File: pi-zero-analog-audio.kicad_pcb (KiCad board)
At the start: 2 copper layers, 65 x 30 mm, 29 parts, among them J1 GPIO, J2 SJ1-3555NG-BE, J3 Screw_Terminal_01x04, U1 LP5907MFX-3.3, U2 74LVC2G34, U3 PAM8403D

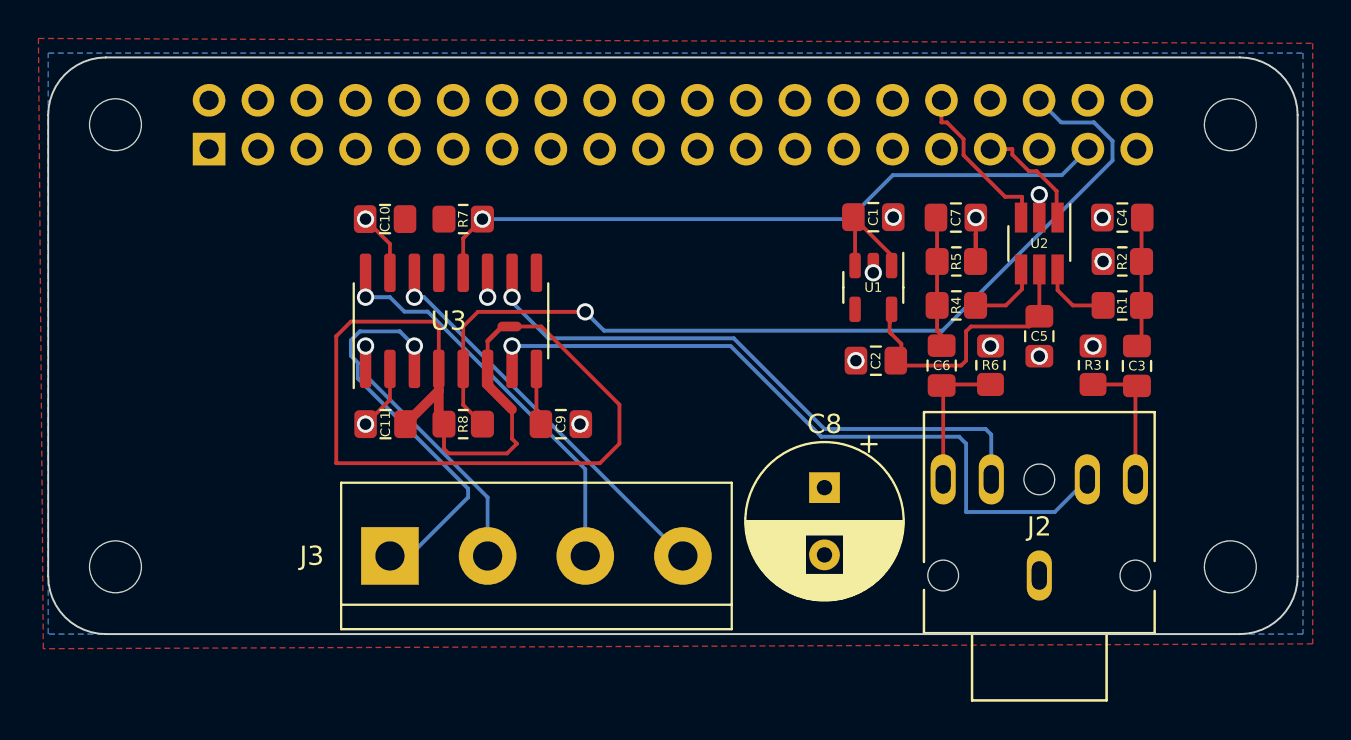
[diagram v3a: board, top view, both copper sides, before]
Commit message: Clearing the mounting holes to avoid accidental short
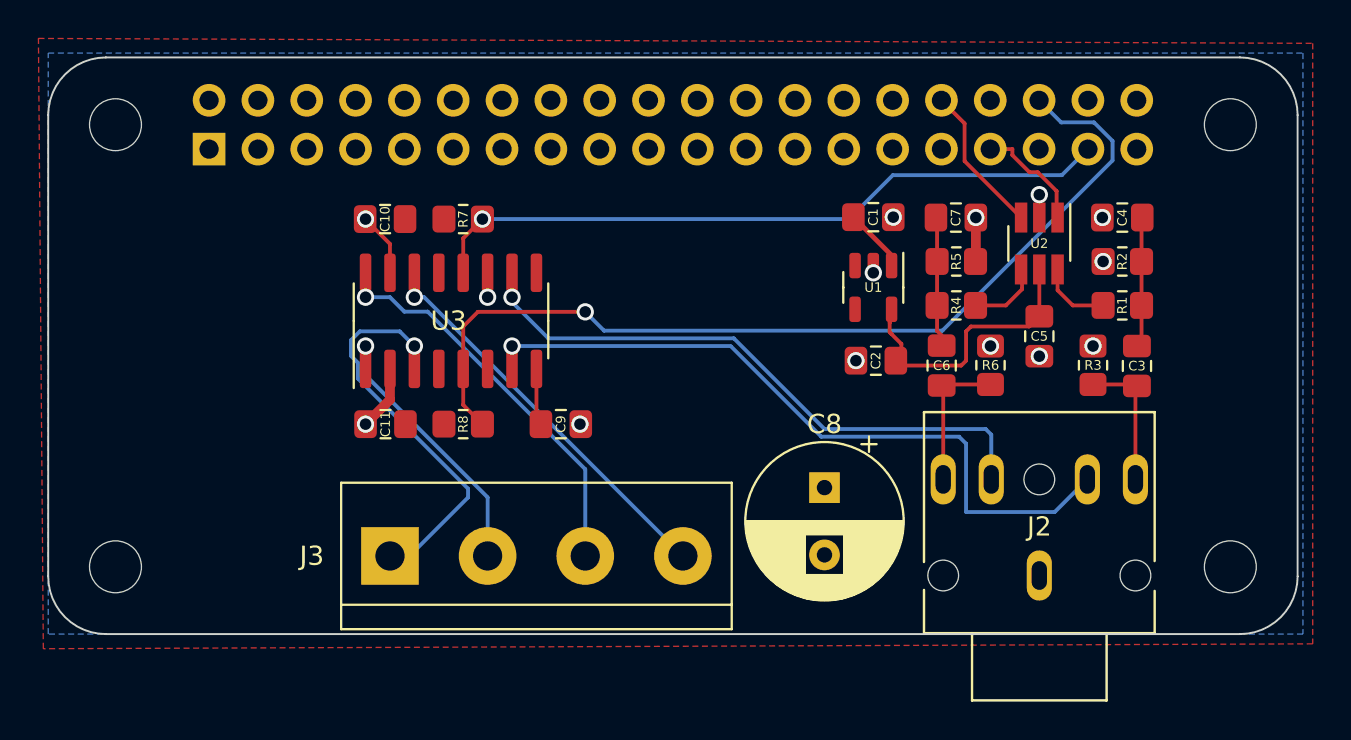
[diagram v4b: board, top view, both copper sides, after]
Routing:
- net +5V: track 62.6 -> 2.81 mm
- net GND: track 9.85 -> 8.98 mm
- net /PWM0: track 8.52 -> 7.82 mm
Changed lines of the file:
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@@
     (fp_circle (center 0 0) (end 2.7 0) (layer "Cmts.User") (width 0.15) (fill none))
     (fp_circle (center 0 0) (end 2.95 0) (layer "F.CrtYd") (width 0.05) (fill none))
-    (pad "" np_thru_hole circle locked (at 0 0) (size 2.7 2.7) (drill 2.7) (layers *.Cu *.Mask))
+    (pad "" np_thru_hole circle locked (at 0 0) (size 2.7 2.7) (drill 2.7) (layers F&B.Cu *.Mask)
+      (clearance 1.625))
   )
   (footprint "Capacitor_SMD:C_0805_2012Metric_Pad1.18x1.45mm_HandSolder" (layer "F.Cu")
@@
     (fp_circle (center 0 0) (end 2.7 0) (layer "Cmts.User") (width 0.15) (fill none))
     (fp_circle (center 0 0) (end 2.95 0) (layer "F.CrtYd") (width 0.05) (fill none))
-    (pad "" np_thru_hole circle locked (at 0 0) (size 2.7 2.7) (drill 2.7) (layers *.Cu *.Mask))
+    (pad "" np_thru_hole circle locked (at 0 0) (size 2.7 2.7) (drill 2.7) (layers F&B.Cu *.Mask)
+      (clearance 1.625))
   )
   (footprint "MountingHole:MountingHole_2.7mm_M2.5" locked (layer "F.Cu")
@@
     (fp_circle (center 0 0) (end 2.7 0) (layer "Cmts.User") (width 0.15) (fill none))
     (fp_circle (center 0 0) (end 2.95 0) (layer "F.CrtYd") (width 0.05) (fill none))
-    (pad "" np_thru_hole circle locked (at 0 0) (size 2.7 2.7) (drill 2.7) (layers *.Cu *.Mask))
+    (pad "" np_thru_hole circle locked (at 0 0) (size 2.7 2.7) (drill 2.7) (layers F&B.Cu *.Mask)
+      (clearance 1.625))
   )
   (footprint "Package_TO_SOT_SMD:SOT-23-5" (layer "F.Cu")
@@
     (fp_circle (center 0 0) (end 2.7 0) (layer "Cmts.User") (width 0.15) (fill none))
     (fp_circle (center 0 0) (end 2.95 0) (layer "F.CrtYd") (width 0.05) (fill none))
-    (pad "" np_thru_hole circle locked (at 0 0) (size 2.7 2.7) (drill 2.7) (layers *.Cu *.Mask))
+    (pad "" np_thru_hole circle locked (at 0 0) (size 2.7 2.7) (drill 2.7) (layers F&B.Cu *.Mask)
+      (clearance 1.625))
   )
   (footprint "Capacitor_SMD:C_0805_2012Metric_Pad1.18x1.45mm_HandSolder" (layer "F.Cu")
@@
   (gr_arc (start 100 73) (mid 100.87868 70.87868) (end 103 70) (layer "Edge.Cuts") (width 0.1))
   (gr_line (start 162 70) (end 103 70) (layer "Edge.Cuts") (width 0.1))
-  (segment (start 148.26 79.1715) (end 148.244 79.1875) (width 0.2) (layer "F.Cu") (net 1))
-  (segment (start 117.78 87.808) (end 116.51 89.078) (width 0.2) (layer "F.Cu") (net 1))
   (segment (start 117.78 79.7015) (end 116.499 78.421) (width 0.2) (layer "F.Cu") (net 1))
-  (segment (start 117.78 86.204) (end 117.78 87.808) (width 0.2) (layer "F.Cu") (net 1))
-  (segment (start 148.244 79.1875) (end 148.244 80.616) (width 0.2) (layer "F.Cu") (net 1))
   (segment (start 117.78 81.204) (end 117.78 79.7015) (width 0.2) (layer "F.Cu") (net 1))
-  (segment (start 148.26 78.33) (end 148.26 79.1715) (width 0.2) (layer "F.Cu") (net 1))
-  (segment (start 148.26 79.1715) (end 148.26 80.013) (width 0.2) (layer "F.Cu") (net 1))
+  (segment (start 148.26 78.33) (end 148.26 80.6) (width 0.508) (layer "F.Cu") (net 1))
+  (segment (start 117.78 86.204) (end 117.78 87.808) (width 0.508) (layer "F.Cu") (net 1))
+  (segment (start 117.78 87.808) (end 116.51 89.078) (width 0.508) (layer "F.Cu") (net 1))
   (via (at 127.6645 89.078) (size 0.9) (drill 0.6) (layers "F.Cu" "B.Cu") (net 1))
   (via (at 154.88 80.616) (size 0.9) (drill 0.6) (layers "F.Cu" "B.Cu") (net 1))
@@
   (segment (start 143.876 84.3961) (end 143.776 84.2961) (width 0.2) (layer "F.Cu") (net 2))
   (segment (start 151.562 83.4685) (end 151.562 81.03) (width 0.2) (layer "F.Cu") (net 2))
-  (segment (start 147.62 75.0856) (end 149.784 77.2499) (width 0.2) (layer "F.Cu") (net 24))
-  (segment (start 147.62 74.2426) (end 147.62 75.0856) (width 0.2) (layer "F.Cu") (net 24))
-  (segment (start 146.47 72.23) (end 146.47 73.3801) (width 0.2) (layer "F.Cu") (net 24))
-  (segment (start 146.47 73.3801) (end 146.758 73.3801) (width 0.2) (layer "F.Cu") (net 24))
-  (segment (start 150.662 77.2499) (end 150.662 78.33) (width 0.2) (layer "F.Cu") (net 24))
-  (segment (start 146.758 73.3801) (end 147.62 74.2426) (width 0.2) (layer "F.Cu") (net 24))
-  (segment (start 149.784 77.2499) (end 150.662 77.2499) (width 0.2) (layer "F.Cu") (net 24))
+  (segment (start 146.47 72.23) (end 147.674 73.434) (width 0.2) (layer "F.Cu") (net 24))
+  (segment (start 147.674 73.434) (end 147.674 75.392) (width 0.2) (layer "F.Cu") (net 24))
+  (segment (start 147.674 75.392) (end 150.612 78.33) (width 0.2) (layer "F.Cu") (net 24))
+  (segment (start 151.48 75.974) (end 152.462 76.956) (width 0.2) (layer "F.Cu") (net 25))
+  (segment (start 150.16 74.77) (end 150.16 75.082714) (width 0.2) (layer "F.Cu") (net 25))
+  (segment (start 152.462 76.956) (end 152.462 78.33) (width 0.2) (layer "F.Cu") (net 25))
+  (segment (start 150.16 75.082714) (end 151.051286 75.974) (width 0.2) (layer "F.Cu") (net 25))
+  (segment (start 151.051286 75.974) (end 151.48 75.974) (width 0.2) (layer "F.Cu") (net 25))
   (segment (start 149.01 74.77) (end 150.16 74.77) (width 0.2) (layer "F.Cu") (net 25))
-  (segment (start 150.16 74.77) (end 150.16 75.0576) (width 0.2) (layer "F.Cu") (net 25))
-  (segment (start 151.426 75.9201) (end 152.462 76.956) (width 0.2) (layer "F.Cu") (net 25))
-  (segment (start 150.16 75.0576) (end 151.023 75.9201) (width 0.2) (layer "F.Cu") (net 25))
-  (segment (start 152.462 76.956) (end 152.462 78.33) (width 0.2) (layer "F.Cu") (net 25))
-  (segment (start 151.023 75.9201) (end 151.426 75.9201) (width 0.2) (layer "F.Cu") (net 25))
-  (segment (start 122.86 84.76) (end 123.622 83.998) (width 0.254) (layer "F.Cu") (net 27))
-  (segment (start 123.622 83.998) (end 124.384 83.998) (width 0.508) (layer "F.Cu") (net 27))
-  (segment (start 129.718 90.094) (end 128.702 91.11) (width 0.2) (layer "F.Cu") (net 27))
-  (segment (start 114.986 91.11) (end 114.986 84.506) (width 0.2) (layer "F.Cu") (net 27))
-  (segment (start 114.986 84.506) (end 115.748 83.744) (width 0.2) (layer "F.Cu") (net 27))
-  (segment (start 122.86 86.204) (end 122.86 84.76) (width 0.2) (layer "F.Cu") (net 27))
-  (segment (start 123.876 90.602) (end 120.828 90.602) (width 0.2) (layer "F.Cu") (net 27))
-  (segment (start 122.86 87.046) (end 124.13 88.316) (width 0.508) (layer "F.Cu") (net 27))
-  (segment (start 120.32 86.204) (end 120.32 87.343) (width 0.2) (layer "F.Cu") (net 27))
-  (segment (start 120.828 90.602) (end 120.59 90.364) (width 0.2) (layer "F.Cu") (net 27))
-  (segment (start 124.384 90.094) (end 124.13 89.84) (width 0.2) (layer "F.Cu") (net 27))
-  (segment (start 124.384 83.998) (end 125.654 83.998) (width 0.2) (layer "F.Cu") (net 27))
-  (segment (start 120.32 86.204) (end 120.32 88.808) (width 0.508) (layer "F.Cu") (net 27))
-  (segment (start 125.654 83.998) (end 129.718 88.062) (width 0.2) (layer "F.Cu") (net 27))
-  (segment (start 128.702 91.11) (end 114.986 91.11) (width 0.2) (layer "F.Cu") (net 27))
-  (segment (start 120.32 87.343) (end 118.585 89.078) (width 0.508) (layer "F.Cu") (net 27))
-  (segment (start 120.59 90.364) (end 120.59 89.078) (width 0.2) (layer "F.Cu") (net 27))
-  (segment (start 124.384 90.094) (end 123.876 90.602) (width 0.2) (layer "F.Cu") (net 27))
-  (segment (start 115.748 83.744) (end 120.066 83.744) (width 0.2) (layer "F.Cu") (net 27))
-  (segment (start 143.876 80.2975) (end 141.8885 78.31) (width 0.2) (layer "F.Cu") (net 27))
-  (segment (start 141.976 80.8285) (end 141.976 78.3975) (width 0.2) (layer "F.Cu") (net 27))
-  (segment (start 120.32 83.998) (end 120.32 86.204) (width 0.2) (layer "F.Cu") (net 27))
-  (segment (start 129.718 88.062) (end 129.718 90.094) (width 0.2) (layer "F.Cu") (net 27))
-  (segment (start 124.13 89.84) (end 124.13 88.316) (width 0.2) (layer "F.Cu") (net 27))
-  (segment (start 120.066 83.744) (end 120.32 83.998) (width 0.2) (layer "F.Cu") (net 27))
+  (segment (start 141.8885 78.31) (end 143.876 80.2975) (width 0.254) (layer "F.Cu") (net 27))
   (segment (start 156.562 87.169) (end 156.562 91.952) (width 0.2) (layer "F.Cu") (net 30))
   (segment (start 154.356 87.014) (end 156.567 87.014) (width 0.2) (layer "F.Cu") (net 30))
@@
   (segment (start 121.59 83.998) (end 122.352 83.236) (width 0.2) (layer "F.Cu") (net 44))
   (segment (start 121.59 86.204) (end 121.59 83.998) (width 0.2) (layer "F.Cu") (net 44))
-  (segment (start 121.59 86.204) (end 121.59 88.078) (width 0.2) (layer "F.Cu") (net 44))
-  (segment (start 121.59 88.078) (end 122.59 89.078) (width 0.2) (layer "F.Cu") (net 44))
+  (segment (start 121.59 88.078) (end 121.59 86.204) (width 0.2) (layer "F.Cu") (net 44))
+  (segment (start 122.59 89.078) (end 121.59 88.078) (width 0.2) (layer "F.Cu") (net 44))
   (via (at 127.94 83.236) (size 0.9) (drill 0.6) (layers "F.Cu" "B.Cu") (net 44))
   (segment (start 155.372 75.362) (end 155.372 74.346) (width 0.2) (layer "B.Cu") (net 44))
@@
   (zone (net 27) (net_name "+5V") (layer "F.Cu") (hatch edge 0.508)
     (connect_pads (clearance 0.508))
-    (min_thickness 0.254) (filled_areas_thickness no)
+    (min_thickness 0.2) (filled_areas_thickness no)
     (fill yes (thermal_gap 0.508) (thermal_bridge_width 0.508))
     (polygon

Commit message: Capacitor and resistor on the amplifier input, as per PAM8403 specs
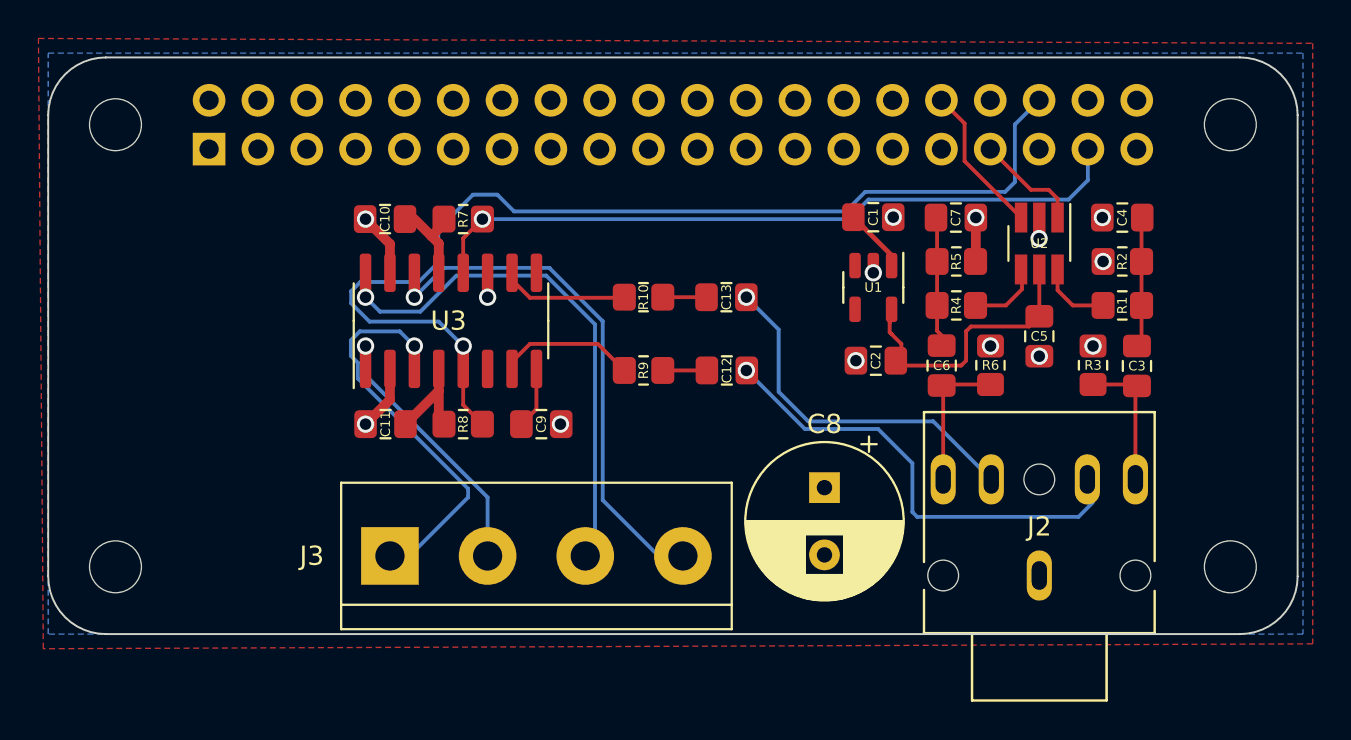
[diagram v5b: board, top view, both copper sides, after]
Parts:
- added C12: 470n, Capacitor_SMD:C_0805_2012Metric_Pad1.18x1.45mm_HandSolder, F.Cu at (135.3, 86.3)
- added C13: 470n, Capacitor_SMD:C_0805_2012Metric_Pad1.18x1.45mm_HandSolder, F.Cu at (135.3, 82.5)
- added R10: 150k, Resistor_SMD:R_0805_2012Metric_Pad1.20x1.40mm_HandSolder, F.Cu at (131.0, 82.5)
- added R9: 150k, Resistor_SMD:R_0805_2012Metric_Pad1.20x1.40mm_HandSolder, F.Cu at (131.0, 86.3)
- moved C9 1.02 mm to (125.7, 89.1)
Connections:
- U3 pad 10: /AMP_R -> Net-(R10-Pad1)
- U3 pad 7: /AMP_L -> Net-(R9-Pad1)
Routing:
- net /AMP_L: track 37.4 -> 23.0 mm
- net /AMP_R: track 31.6 -> 18.6 mm
- net +5V: track 2.81 -> 13.2 mm
- net Net-(R9-Pad1): track 0.00 -> 6.80 mm
- net Net-(R10-Pad1): track 0.00 -> 6.20 mm
- net /R+: track 19.7 -> 25.6 mm
- net /MUTE: track 49.4 -> 55.2 mm
- net /R-: track 19.5 -> 25.0 mm
- net Net-(C12-Pad1): track 0.00 -> 2.30 mm
- net Net-(C13-Pad1): track 0.00 -> 2.28 mm
- net /SHDN: track 36.2 -> 37.2 mm
- net Net-(C9-Pad1): track 2.64 -> 3.20 mm

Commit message: The resistor should be max 142k as per specs
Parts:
- R10, R9: value 150k -> 140k
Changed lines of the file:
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@@
       (effects (font (size 0.5 0.5) (thickness 0.125)))
     )
-    (fp_text value "150k" (at 0 1.65) (layer "F.Fab")
+    (fp_text value "140k" (at 0 1.65) (layer "F.Fab")
       (effects (font (size 1 1) (thickness 0.15)))
     )
@@
       (effects (font (size 0.5 0.5) (thickness 0.125)))
     )
-    (fp_text value "150k" (at 0 1.65) (layer "F.Fab")
-      (effects (font (size 1 1) (thickness 0.15)))
-    )
+    (fp_text value "140k" (at 0 1.65) (layer "F.Fab")
+      (effects (font (size 1 1) (thickness 0.15)))
+    )

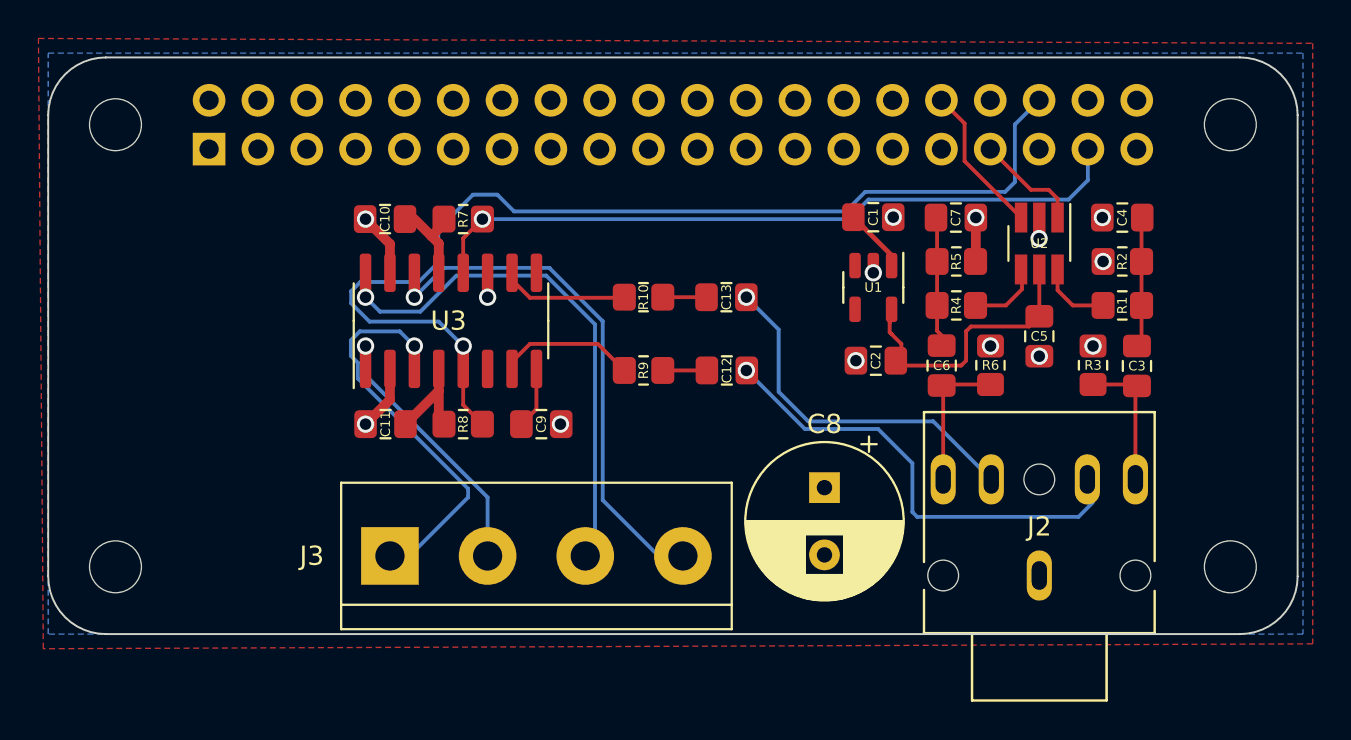
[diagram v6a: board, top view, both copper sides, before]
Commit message: Some footprint changes
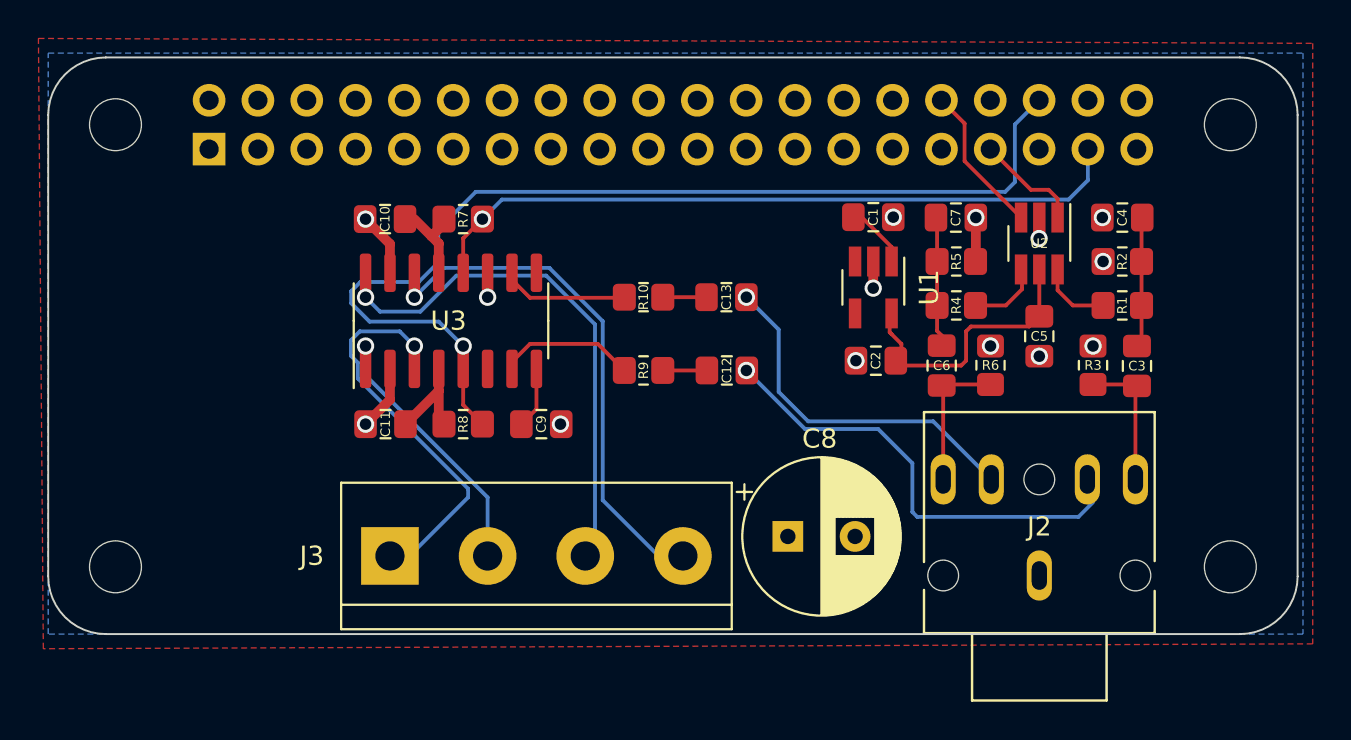
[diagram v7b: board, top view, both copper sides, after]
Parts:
- U1: footprint Package_TO_SOT_SMD:SOT-23-5 -> Package_TO_SOT_SMD:SOT-23-5_HandSoldering
- moved C8 3.18 mm to (138.5, 94.9), turned to 0 degrees
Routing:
- net GND: track 8.98 -> 10.4 mm
- net /MUTE: track 55.2 -> 54.5 mm
